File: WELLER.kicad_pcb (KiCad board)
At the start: 2 copper layers, 20 x 100 mm, 57 parts, among them J1 Jack-DC, J2 AudioJack3_Ground_SwitchTR, J3 jtag conector, J4 Conn_01x04_Female, Q1 DMP2018LFK, SW1 SW_Push_SPDT, SW2 SW_Push, SW3 SW_Push, U1 AP1117-33, U2 LTC4440ES6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

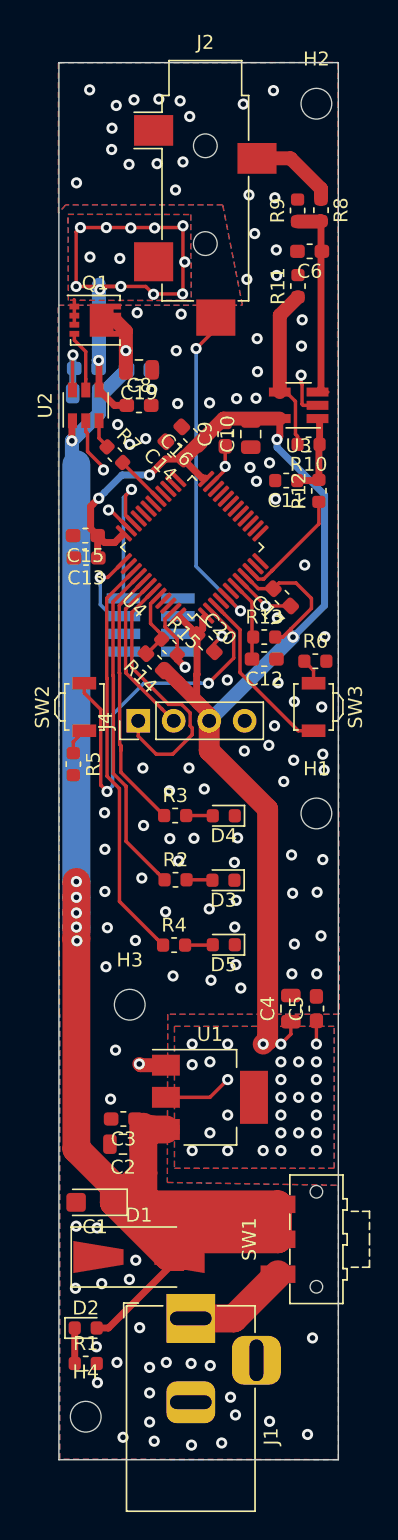
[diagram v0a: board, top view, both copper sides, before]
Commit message: dodanie pullup do i2c i screenow
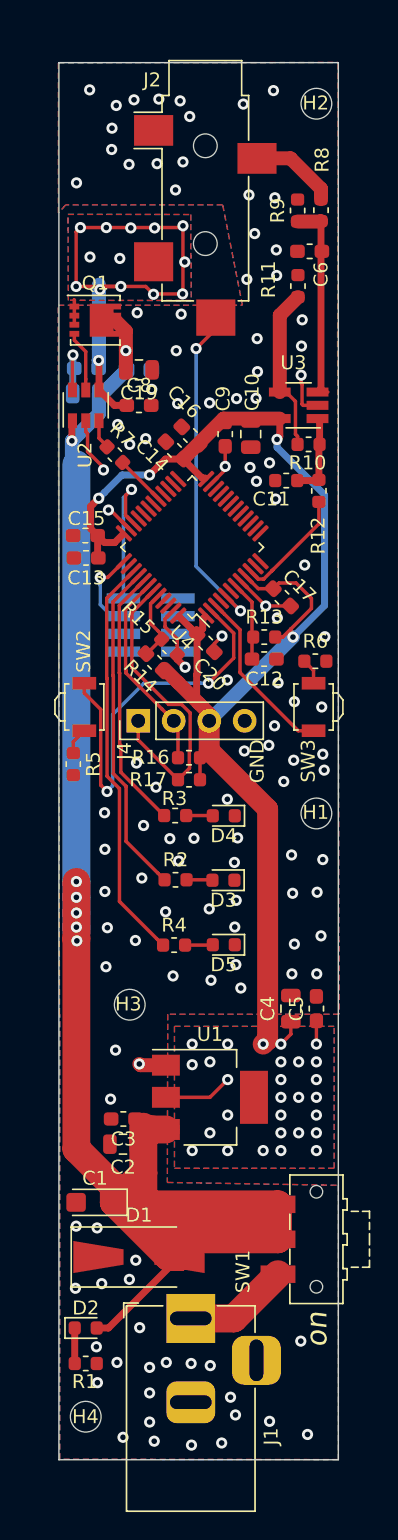
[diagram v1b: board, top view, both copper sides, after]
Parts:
- added R16: 10k, Resistor_SMD:R_0603_1608Metric, F.Cu at (129.3, 74.8)
- added R17: 10k, Resistor_SMD:R_0603_1608Metric, F.Cu at (129.3, 76.3)
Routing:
- net /stm32/sda: track 19.3 -> 22.2 mm
- net /stm32/scl: track 11.8 -> 14.5 mm
- net /tip_driving/3.3V_analog: track 110.3 -> 112.8 mm
- net GND: vias 122 -> 121
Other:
- board text added: "GND"
- board text added: "Weller_RT_tip_solder 05.2019"
- board text added: "k0201"
- board text added: "on"

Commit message: poprawki na sch
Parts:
- J3: value jtag conector -> Conn_02x04_Odd_Even
- U3: footprint Package_TO_SOT_SMD:SOT-23-5_HandSoldering -> TO_SOT_Packages_SMD:SOT-23-6
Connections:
- J3 pad 1: (no net) -> GND
- J3 pad 2: /stm32/SWDIO -> /stm32/nRST
- J3 pad 6: (no net) -> /stm32/SWDIO
- J3 pad 8: (no net) -> /stm32/3_3v
- U4 pad 11: (no net) -> Net-(U4-Pad11)
- U4 pad 12: (no net) -> Net-(U4-Pad12)
- U4 pad 13: (no net) -> Net-(U4-Pad13)
- U4 pad 14: (no net) -> Net-(U4-Pad14)
- U4 pad 15: (no net) -> Net-(U4-Pad15)
- U4 pad 16: (no net) -> Net-(U4-Pad16)
- U4 pad 17: (no net) -> Net-(U4-Pad17)
- U4 pad 18: (no net) -> Net-(U4-Pad18)
- U4 pad 19: (no net) -> Net-(U4-Pad19)
- U4 pad 20: (no net) -> Net-(U4-Pad20)
- U4 pad 21: (no net) -> Net-(U4-Pad21)
- U4 pad 22: (no net) -> Net-(U4-Pad22)
- U4 pad 25: (no net) -> Net-(U4-Pad25)
- U4 pad 26: (no net) -> Net-(U4-Pad26)
- U4 pad 27: (no net) -> Net-(U4-Pad27)
- U4 pad 28: (no net) -> Net-(U4-Pad28)
- U4 pad 30: (no net) -> Net-(U4-Pad30)
- U4 pad 31: (no net) -> Net-(U4-Pad31)
- U4 pad 32: (no net) -> Net-(U4-Pad32)
- U4 pad 33: (no net) -> Net-(U4-Pad33)
- U4 pad 38: (no net) -> Net-(U4-Pad38)
- U4 pad 4: (no net) -> Net-(U4-Pad4)
- U4 pad 45: (no net) -> Net-(U4-Pad45)
- U4 pad 46: (no net) -> Net-(U4-Pad46)
- U4 pad 6: (no net) -> Net-(U4-Pad6)
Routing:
- net /tip_driving/3.3V_analog: track 112.8 -> 113.7 mm
- net Net-(C6-Pad1): track 14.8 -> 14.0 mm

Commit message: duży update, drc przechodzi
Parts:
- removed H1, H2, H3, H4: MountingHole, MountingHole:MountingHole_2.2mm_M2
- added R18: 560k, Resistor_SMD:R_0603_1608Metric, B.Cu at (124.3, 88.1)
- added R19: 100k, Resistor_SMD:R_0603_1608Metric, B.Cu at (124.3, 89.7)
- added U5: SM353LT, Package_TO_SOT_SMD:SOT-23, B.Cu at (129.7, 91.1)
- C12, R13: moved to B.Cu
- J1: footprint Connector_BarrelJack:BarrelJack_Horizontal -> symbols:jackDC_cutout
- J2: value AudioJack3_Ground_SwitchTR -> AudioJack3_Ground_SwitchR; footprint Connector_Audio:Jack_3.5mm_CUI_SJ-3524-SMT_Horizontal -> symbols:Jack Audio 1503 20; moved to B.Cu
- J3: value Conn_02x04_Odd_Even -> debug+programing; footprint Connector_PinHeader_1.27mm:PinHeader_2x04_P1.27mm_Vertical_SMD -> Connector_PinHeader_1.27mm:PinHeader_2x05_P1.27mm_Vertical_SMD
- J4: value Conn_01x04_Female -> I2c oled
- R7: footprint Resistor_SMD:R_0603_1608Metric -> Resistor_SMD:R_1206_3216Metric
- moved J2 8.06 mm to (131.4, 25.5), turned to 90 degrees
- moved D2 6.76 mm to (122.1, 122.3)
- moved D1 6.56 mm to (122.7, 116.3), turned to 90 degrees
- moved J3 6.13 mm to (129.2, 59.7), turned to 270 degrees
- moved C2 5.92 mm to (124.4, 108.3)
- moved R1 5.92 mm to (122.0, 124.0)
- moved C3 5.91 mm to (124.2, 106.5)
- moved R13 4.78 mm to (134.6, 61.3)
- moved C12 4.78 mm to (134.7, 62.9)
- moved C1 3.19 mm to (125.0, 104.5)
- moved J1 3.12 mm to (130.2, 111.9), turned to 0 degrees
- moved C13 1.32 mm to (121.3, 61.6), turned to 270 degrees
- moved SW1 1.19 mm to (137.8, 108.2)
- moved R7 1.10 mm to (123.2, 53.8), turned to 270 degrees
- moved R5 1.01 mm to (122.0, 75.1)
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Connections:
- net /tip_driving/12V renamed /stm32/12V
- J2 pad R: /tip_driving/termocouple+ -> /tip_driving/heater
- J2 pad S: GND -> /tip_driving/termocouple+
- J3 pad 1: GND -> /tip_driving/3.3V_analog
- J3 pad 2: /stm32/nRST -> /stm32/SWDIO
- J3 pad 3: GND -> /stm32/usart_rx
- J3 pad 5: GND -> /stm32/usart_tx
- J3 pad 6: /stm32/SWDIO -> (no net)
- J3 pad 7: GND -> /stm32/usart_ck
- J3 pad 8: /stm32/3_3v -> (no net)
- U4 pad 10: /stm32/termocouple -> /stm32/hall_in
- U4 pad 11: Net-(U4-Pad11) -> /stm32/input_divider
- U4 pad 12: Net-(U4-Pad12) -> (no net)
- U4 pad 13: Net-(U4-Pad13) -> /stm32/termocouple
- U4 pad 14: Net-(U4-Pad14) -> (no net)
- U4 pad 15: Net-(U4-Pad15) -> (no net)
- U4 pad 16: Net-(U4-Pad16) -> (no net)
- U4 pad 17: Net-(U4-Pad17) -> (no net)
- U4 pad 18: Net-(U4-Pad18) -> (no net)
- U4 pad 19: Net-(U4-Pad19) -> /stm32/weller_con1
- U4 pad 20: Net-(U4-Pad20) -> (no net)
- U4 pad 21: Net-(U4-Pad21) -> (no net)
- U4 pad 22: Net-(U4-Pad22) -> (no net)
- U4 pad 25: Net-(U4-Pad25) -> (no net)
- U4 pad 26: Net-(U4-Pad26) -> (no net)
- U4 pad 27: Net-(U4-Pad27) -> (no net)
- U4 pad 28: Net-(U4-Pad28) -> (no net)
- U4 pad 29: /tip_driving/HeaterDrivePWM -> /stm32/usart_rx
- U4 pad 30: Net-(U4-Pad30) -> /stm32/usart_tx
- U4 pad 31: Net-(U4-Pad31) -> /stm32/usart_ck
- U4 pad 32: Net-(U4-Pad32) -> /tip_driving/HeaterDrivePWM
- U4 pad 33: Net-(U4-Pad33) -> (no net)
- U4 pad 38: Net-(U4-Pad38) -> (no net)
- U4 pad 4: Net-(U4-Pad4) -> (no net)
- U4 pad 45: Net-(U4-Pad45) -> (no net)
- U4 pad 46: Net-(U4-Pad46) -> (no net)
- U4 pad 5: /stm32/weller_con1 -> (no net)
- U4 pad 6: Net-(U4-Pad6) -> (no net)
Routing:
- net GND: track 25.9 -> 65.3 mm, vias 121 -> 78
- net /stm32/input_divider: track 0.00 -> 39.1 mm, vias 0 -> 1
- net /stm32/hall_in: track 0.00 -> 38.5 mm, vias 0 -> 1
- net /stm32/12V: track 132.7 -> 104.2 mm, vias 7 -> 12
- net /stm32/usart_ck: track 0.00 -> 12.7 mm, vias 0 -> 1
- net /tip_driving/heater: track 38.4 -> 50.7 mm, vias 14 -> 10
- net /tip_driving/3.3V_analog: track 113.7 -> 125.3 mm, vias 32 -> 31
- net /stm32/weller_con1: track 24.4 -> 34.9 mm, vias 2 -> 1
- net /stm32/usart_tx: track 0.00 -> 9.75 mm, vias 0 -> 1
- net /stm32/usart_rx: track 0.00 -> 6.02 mm, vias 0 -> 1
- net /stm32/nRST: track 5.72 -> 9.78 mm, vias 0 -> 1
- net /stm32/termocouple: track 8.49 -> 5.11 mm
- net /stm32/SWCLK: track 6.11 -> 9.07 mm
- net /tip_driving/termocouple+: track 6.22 -> 9.06 mm, vias 0 -> 1
- net Net-(J1-Pad1): track 7.55 -> 6.14 mm
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- added copper zone on F.Cu, net /stm32/12V
- removed copper zone on B.Cu, net /tip_driving/heater
- removed copper zone on F.Cu, net /tip_driving/heater
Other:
- outline, holes or cut-outs redrawn
- board text added: "Weller_RT_tip_solder_v1 05.2019"
- board text removed: "Weller_RT_tip_solder 05.2019"

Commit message: dodanie pomiaru napięcia zasilającego grzałkę
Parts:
- added C21: 100n, Capacitor_SMD:C_0603_1608Metric_Pad1.05x0.95mm_HandSolder, F.Cu at (130.3, 46.6)
- added C22: 100n, Capacitor_SMD:C_0603_1608Metric_Pad1.05x0.95mm_HandSolder, F.Cu at (127.8, 45.2)
- added C23: 100n, Capacitor_SMD:C_0603_1608Metric_Pad1.05x0.95mm_HandSolder, F.Cu at (127.8, 41.9)
- added R20: 56k, Resistor_SMD:R_0603_1608Metric_Pad1.05x0.95mm_HandSolder, F.Cu at (127.8, 43.6)
- added R21: 10, Resistor_SMD:R_0603_1608Metric_Pad1.05x0.95mm_HandSolder, F.Cu at (132.6, 46.6)
- added R22: R, Resistor_SMD:R_0603_1608Metric_Pad1.05x0.95mm_HandSolder, F.Cu at (134.2, 46.6)
- added R23: R, Resistor_SMD:R_0603_1608Metric_Pad1.05x0.95mm_HandSolder, F.Cu at (134.2, 43.1)
- added U6: LMC7101-AYM5-TR, Package_TO_SOT_SMD:SOT-23-5, F.Cu at (131.5, 43.1)
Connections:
- U4 pad 14: (no net) -> /stm32/input_sense
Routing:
- net /stm32/input_sense: track 0.00 -> 16.1 mm, vias 0 -> 2
- net GND: track 65.3 -> 77.4 mm, vias 78 -> 81
- net /stm32/12V: track 104.2 -> 113.3 mm
- net Net-(R21-Pad1): track 0.00 -> 8.98 mm
- net Net-(J1-Pad1): track 6.14 -> 10.3 mm
- net Net-(C21-Pad1): track 0.00 -> 3.54 mm
- net Net-(R21-Pad2): track 0.00 -> 1.58 mm
- net /stm32/weller_con1: track 34.9 -> 33.5 mm

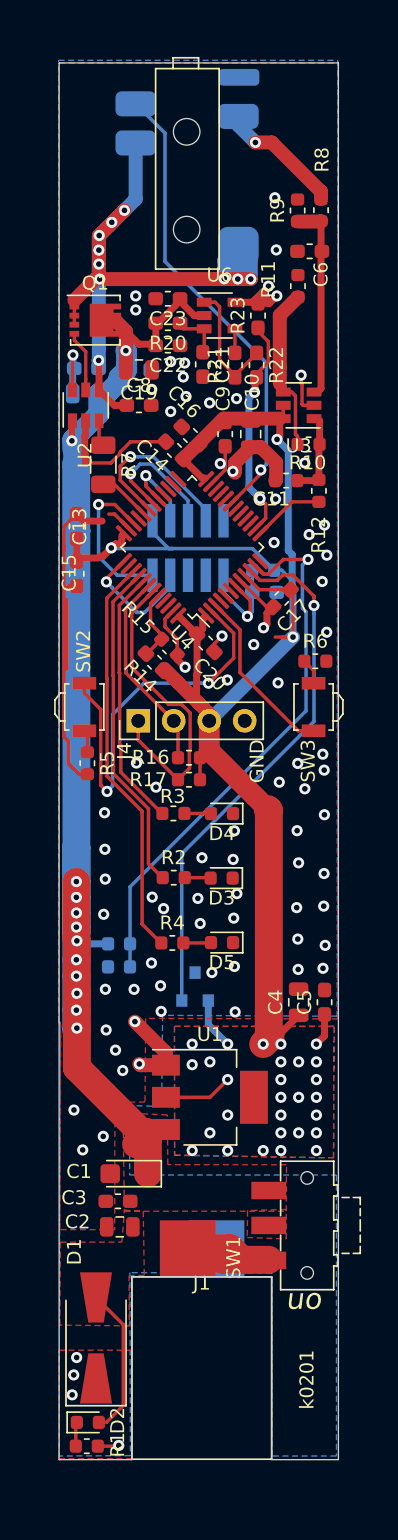
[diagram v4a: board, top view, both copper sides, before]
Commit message: poprawki głownie na pcb zaokrąglenie strony z grotem
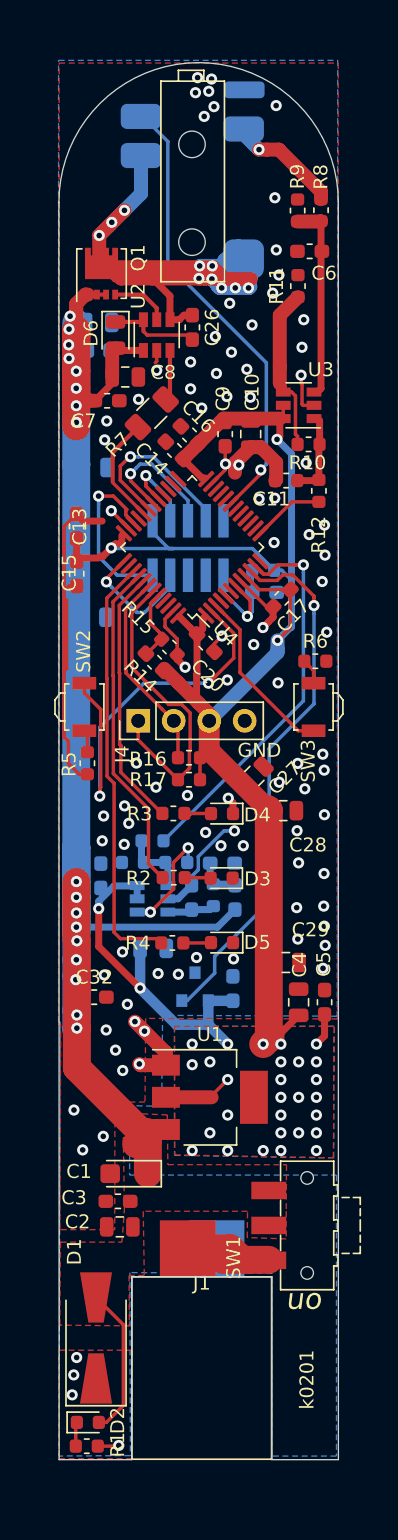
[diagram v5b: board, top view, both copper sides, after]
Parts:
- removed R18: 560k, Resistor_SMD:R_0603_1608Metric
- removed R19: 100k, Resistor_SMD:R_0603_1608Metric
- added C24: n.c., Capacitor_SMD:C_0603_1608Metric, B.Cu at (125.3, 82.2)
- added C25: 100n, Capacitor_SMD:C_0603_1608Metric_Pad1.05x0.95mm_HandSolder, B.Cu at (132.4, 91.3)
- added C26: 100n, Capacitor_SMD:C_0603_1608Metric_Pad1.05x0.95mm_HandSolder, F.Cu at (129.6, 44.0)
- added C27: 10u, Capacitor_SMD:C_0805_2012Metric, F.Cu at (134.0, 76.0)
- added C28: 10u, Capacitor_SMD:C_0805_2012Metric, F.Cu at (136.1, 78.5)
- added C29: 10u, Capacitor_SMD:C_0805_2012Metric, F.Cu at (136.2, 89.4)
- added C30: 1u, Capacitor_SMD:C_0805_2012Metric, B.Cu at (122.5, 54.0)
- added C31: 1u, Capacitor_SMD:C_0805_2012Metric, B.Cu at (122.4, 64.7)
- added C32: 100n, Capacitor_SMD:C_0603_1608Metric_Pad1.05x0.95mm_HandSolder, F.Cu at (122.5, 91.9)
- added R24: 1k, Resistor_SMD:R_0603_1608Metric, B.Cu at (126.7, 80.7)
- C19, C21, C22: moved to B.Cu
- C23: footprint Capacitor_SMD:C_0603_1608Metric_Pad1.05x0.95mm_HandSolder -> Capacitor_SMD:C_0805_2012Metric; moved to B.Cu
- C7: moved to F.Cu
- C8: value 100n -> 10uF; footprint Capacitor_SMD:C_0603_1608Metric_Pad1.05x0.95mm_HandSolder -> Capacitor_SMD:C_0805_2012Metric
- D6: value 1n4148 -> 1N4148; moved to F.Cu
- R20: value 56k -> 1.5Meg; moved to B.Cu
- R21: value 10 -> 300k; moved to B.Cu
- R22: value R -> 56k; footprint Resistor_SMD:R_0603_1608Metric_Pad1.05x0.95mm_HandSolder -> Resistor_SMD:R_0603_1608Metric; moved to B.Cu
- R23: value R -> 10; footprint Resistor_SMD:R_0603_1608Metric_Pad1.05x0.95mm_HandSolder -> Resistor_SMD:R_0603_1608Metric; moved to B.Cu
- U2: value LTC4440ES6 -> LTC4440IS6
- U6: value LMC7101-AYM5-TR -> MCP603-xCH; footprint Package_TO_SOT_SMD:SOT-23-5 -> Package_TO_SOT_SMD:SOT-23-6; moved to B.Cu
- moved C23 46.5 mm to (126.8, 88.4)
- moved U6 42.0 mm to (126.7, 84.8), turned to 180 degrees
- moved R20 41.4 mm to (132.6, 84.8), turned to 90 degrees
- moved R23 39.6 mm to (128.4, 82.2), turned to 180 degrees
- moved C22 38.3 mm to (123.0, 83.2), turned to 270 degrees
- moved C21 38.2 mm to (129.5, 84.8), turned to 90 degrees
- moved R22 38.1 mm to (131.1, 84.6)
- moved R21 35.7 mm to (131.7, 82.3), turned to 0 degrees
- moved U2 7.15 mm to (127.0, 44.5)
- moved R7 5.06 mm to (126.7, 50.1), turned to 225 degrees
- moved D6 4.70 mm to (124.0, 44.5), turned to 270 degrees
- moved C19 4.45 mm to (122.8, 43.6)
- moved Q1 3.36 mm to (123.0, 40.1), turned to 90 degrees
- moved C18 3.20 mm to (122.8, 45.6)
- moved C7 2.74 mm to (123.5, 49.2)
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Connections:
- C1 pad 1: /stm32/12V -> /tip_driving/12V
- C18 pad 1: /stm32/12V -> /tip_driving/12V
- C19 pad 2: /stm32/12V -> /tip_driving/12V
- C2 pad 1: /stm32/12V -> /tip_driving/12V
- C22 pad 2: /stm32/12V -> /tip_driving/3.3V_analog
- C23 pad 1: /stm32/12V -> GND
- C23 pad 2: GND -> /tip_driving/3.3V_analog
- C3 pad 1: /stm32/12V -> /tip_driving/12V
- C7 pad 1: Net-(C7-Pad1) -> /tip_driving/12V
- C7 pad 2: /tip_driving/heater -> GND
- C8 pad 1: /tip_driving/heater -> GND
- C8 pad 2: GND -> /tip_driving/12V
- D1 pad 2: /stm32/12V -> /tip_driving/12V
- D2 pad 2: /stm32/12V -> /tip_driving/12V
- D6 pad 1: Net-(C7-Pad1) -> Net-(C26-Pad2)
- D6 pad 2: /stm32/12V -> /tip_driving/12V
- Q1 pad 1: /tip_driving/heater -> /tip_driving/12V
- Q1 pad 2: /tip_driving/heater -> /tip_driving/12V
- Q1 pad 3: /tip_driving/heater -> /tip_driving/12V
- Q1 pad 5: /stm32/12V -> /tip_driving/heater
- R20 pad 1: Net-(C21-Pad1) -> /tip_driving/12V
- R20 pad 2: /stm32/12V -> Net-(R20-Pad2)
- R21 pad 1: Net-(R21-Pad1) -> Net-(R20-Pad2)
- R21 pad 2: Net-(R21-Pad2) -> GND
- R22 pad 1: Net-(R21-Pad1) -> Net-(R20-Pad2)
- R22 pad 2: /stm32/input_sense -> Net-(C21-Pad1)
- R23 pad 1: /stm32/input_sense -> Net-(R23-Pad1)
- R23 pad 2: GND -> Net-(C24-Pad1)
- SW1 pad 2: /stm32/12V -> /tip_driving/12V
- SW1 pad 3: /stm32/12V -> /tip_driving/12V
- U1 pad 3: /stm32/12V -> /tip_driving/12V
- U2 pad 1: /stm32/12V -> /tip_driving/12V
- U2 pad 6: Net-(C7-Pad1) -> Net-(C26-Pad2)
- U4 pad 11: /stm32/input_divider -> /stm32/input_sense
- U4 pad 14: /stm32/input_sense -> (no net)
- U6 pad 1: Net-(R21-Pad1) -> Net-(C24-Pad1)
- U6 pad 2: /stm32/12V -> GND
- U6 pad 4: Net-(R21-Pad2) -> Net-(R23-Pad1)
- U6 pad 5: GND -> /tip_driving/3.3V_analog
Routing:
- net /tip_driving/12V: track 0.00 -> 130.9 mm, vias 0 -> 17
- net /stm32/12V: track 113.3 -> 0.00 mm, vias 12 -> 0
- net /stm32/input_divider: track 39.1 -> 0.00 mm, vias 1 -> 0
- net /tip_driving/3.3V_analog: track 125.3 -> 152.6 mm, vias 31 -> 33
- net /stm32/input_sense: track 16.1 -> 27.8 mm, vias 2 -> 1
- net Net-(R21-Pad1): track 8.98 -> 0.00 mm
- net Net-(C7-Pad1): track 7.75 -> 0.00 mm, vias 1 -> 0
- net Net-(R23-Pad1): track 0.00 -> 7.74 mm, vias 0 -> 2
- net /tip_driving/heater: track 50.7 -> 57.5 mm
- net Net-(C26-Pad2): track 0.00 -> 6.64 mm
- net GND: track 77.4 -> 71.6 mm, vias 81 -> 95
- net Net-(C24-Pad1): track 0.00 -> 4.88 mm
- net /tip_driving/HeaterDrivePWM: track 3.76 -> 7.77 mm
- net Net-(R20-Pad2): track 0.00 -> 3.17 mm
- net Net-(R7-Pad1): track 2.06 -> 3.64 mm
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- added copper zone on F.Cu, net /tip_driving/12V
- removed copper zone on F.Cu, net /stm32/12V
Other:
- outline, holes or cut-outs redrawn

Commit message: wyciecie przy gnieździe jack - dodanie 3d gniazda, update jpg
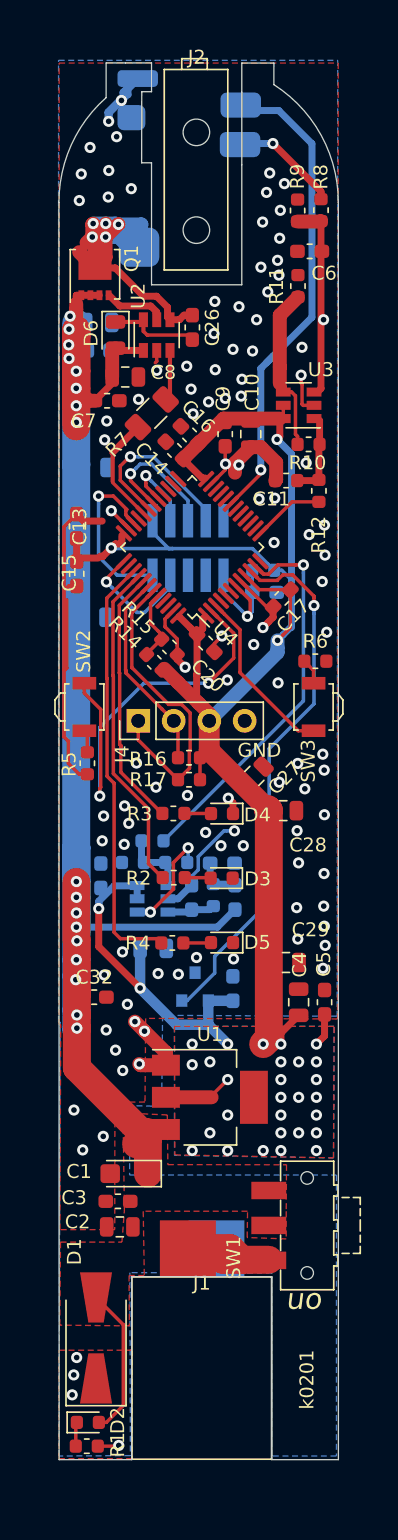
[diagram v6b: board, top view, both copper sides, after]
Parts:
- J2: footprint symbols:Jack Audio 1503 20 -> symbols:Jack Audio150320cutout; moved to F.Cu
- R14: value n.c. -> 10k; footprint Resistor_SMD:R_0603_1608Metric_Pad1.05x0.95mm_HandSolder -> Resistor_SMD:R_0603_1608Metric
- R2, R3, R4: value R -> 220
- moved J2 4.37 mm to (127.5, 25.5)
- moved Q1 0.47 mm to (122.6, 40.1)
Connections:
- J2 pad R: /tip_driving/heater -> /tip_driving/termocouple+
- J2 pad S: /tip_driving/termocouple+ -> GND
- J3 pad 6: (no net) -> Net-(J3-Pad6)
- J3 pad 8: (no net) -> Net-(J3-Pad8)
- U4 pad 12: (no net) -> Net-(U4-Pad12)
- U4 pad 14: (no net) -> Net-(U4-Pad14)
- U4 pad 15: (no net) -> Net-(U4-Pad15)
- U4 pad 16: (no net) -> Net-(U4-Pad16)
- U4 pad 17: (no net) -> Net-(U4-Pad17)
- U4 pad 18: (no net) -> Net-(U4-Pad18)
- U4 pad 20: (no net) -> Net-(U4-Pad20)
- U4 pad 21: (no net) -> Net-(U4-Pad21)
- U4 pad 22: (no net) -> Net-(U4-Pad22)
- U4 pad 25: (no net) -> Net-(U4-Pad25)
- U4 pad 26: (no net) -> Net-(U4-Pad26)
- U4 pad 27: (no net) -> Net-(U4-Pad27)
- U4 pad 28: (no net) -> Net-(U4-Pad28)
- U4 pad 33: (no net) -> Net-(U4-Pad33)
- U4 pad 38: (no net) -> Net-(U4-Pad38)
- U4 pad 4: (no net) -> Net-(U4-Pad4)
- U4 pad 45: (no net) -> Net-(U4-Pad45)
- U4 pad 46: (no net) -> Net-(U4-Pad46)
- U4 pad 5: (no net) -> Net-(U4-Pad5)
- U4 pad 6: (no net) -> Net-(U4-Pad6)
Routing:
- net /tip_driving/heater: track 57.5 -> 26.4 mm, vias 10 -> 5
- net GND: track 71.6 -> 77.6 mm, vias 95 -> 105
- net /tip_driving/termocouple+: track 8.57 -> 7.19 mm
- net /stm32/weller_con1: track 33.2 -> 34.5 mm
- net Net-(C6-Pad1): vias 0 -> 1
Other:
- outline, holes or cut-outs redrawn
